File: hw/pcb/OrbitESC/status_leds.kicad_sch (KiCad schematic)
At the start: 12 parts

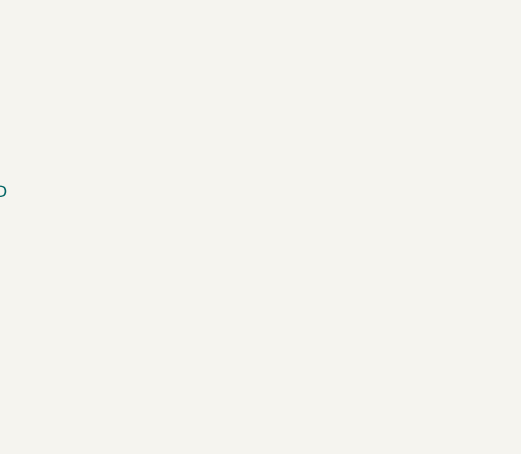
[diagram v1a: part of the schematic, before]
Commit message: Start rework of processor selection after realizing I can't afford manufacturing...
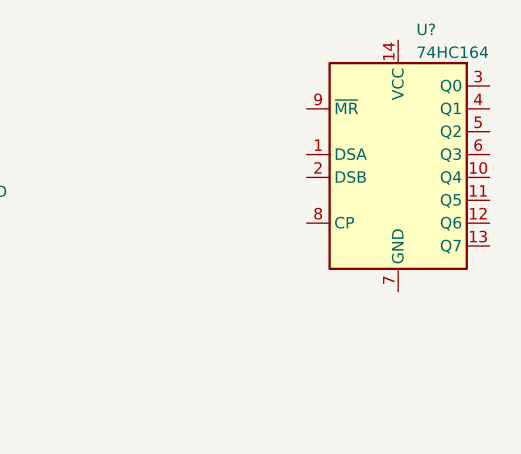
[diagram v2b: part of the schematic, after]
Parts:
- added U?: 74HC164, symbol 74xx:74HC164
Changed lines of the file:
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@@
     (pin "1")
+  )
+  (symbol (lib_id "74xx:74HC164") (at 195.58 71.12 0) (unit 1)
+    (in_bom yes) (on_board yes) (fields_autoplaced)
+    (property "Reference" "U?" (id 0) (at 197.5994 57.2602 0)
+      (effects (font (size 1.27 1.27)) (justify left))
+    )
+    (property "Value" "74HC164" (id 1) (at 197.5994 59.7971 0)
+      (effects (font (size 1.27 1.27)) (justify left))
+    )
+    (property "Footprint" "" (id 2) (at 218.44 78.74 0)
+      (effects (font (size 1.27 1.27)) hide)
+    )
+    (property "Datasheet" "https://assets.nexperia.com/documents/data-sheet/74HC_HCT164.pdf" (id 3) (at 218.44 78.74 0)
+      (effects (font (size 1.27 1.27)) hide)
+    )
+    (property "DigiKey" "MC74HC164ADR2GOSCT-ND" (id 4) (at 195.58 71.12 0)
+      (effects (font (size 1.27 1.27)) hide)
+    )
+    (pin "1")
+    (pin "10")
+    (pin "11")
+    (pin "12")
+    (pin "13")
+    (pin "14")
+    (pin "2")
+    (pin "3")
+    (pin "4")
+    (pin "5")
+    (pin "6")
+    (pin "7")
+    (pin "8")
+    (pin "9")
   )
   (symbol (lib_id "Device:LED") (at 116.84 72.39 90) (unit 1)

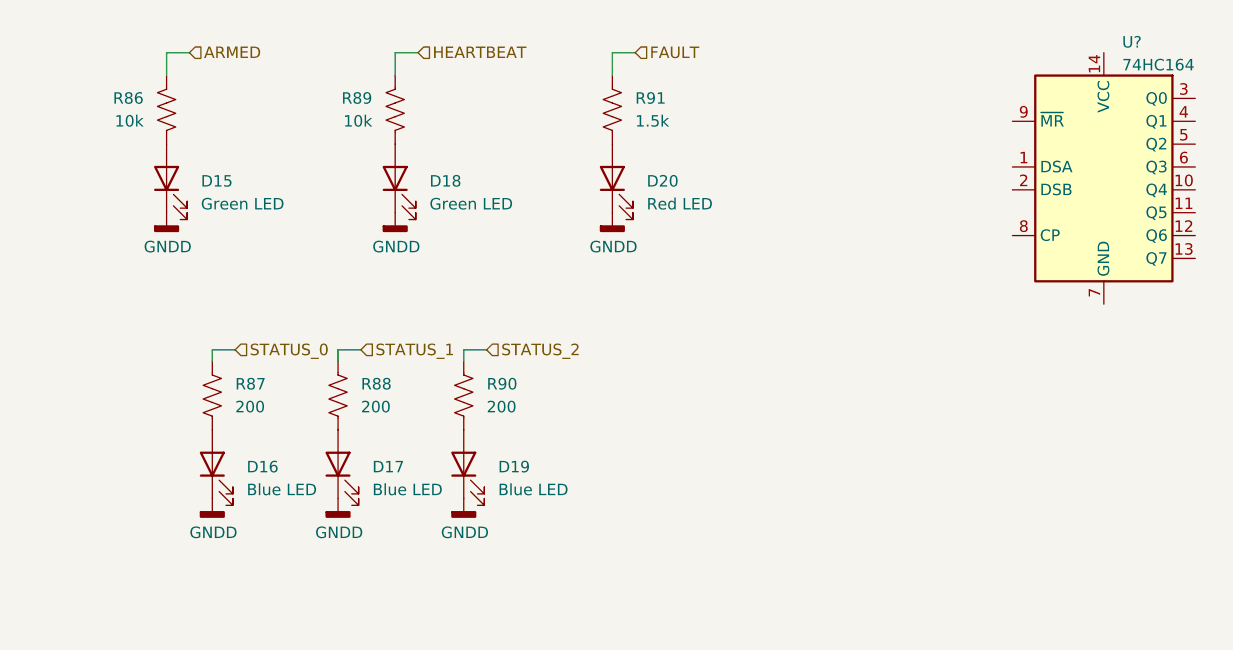
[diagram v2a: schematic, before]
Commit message: Rework new processor
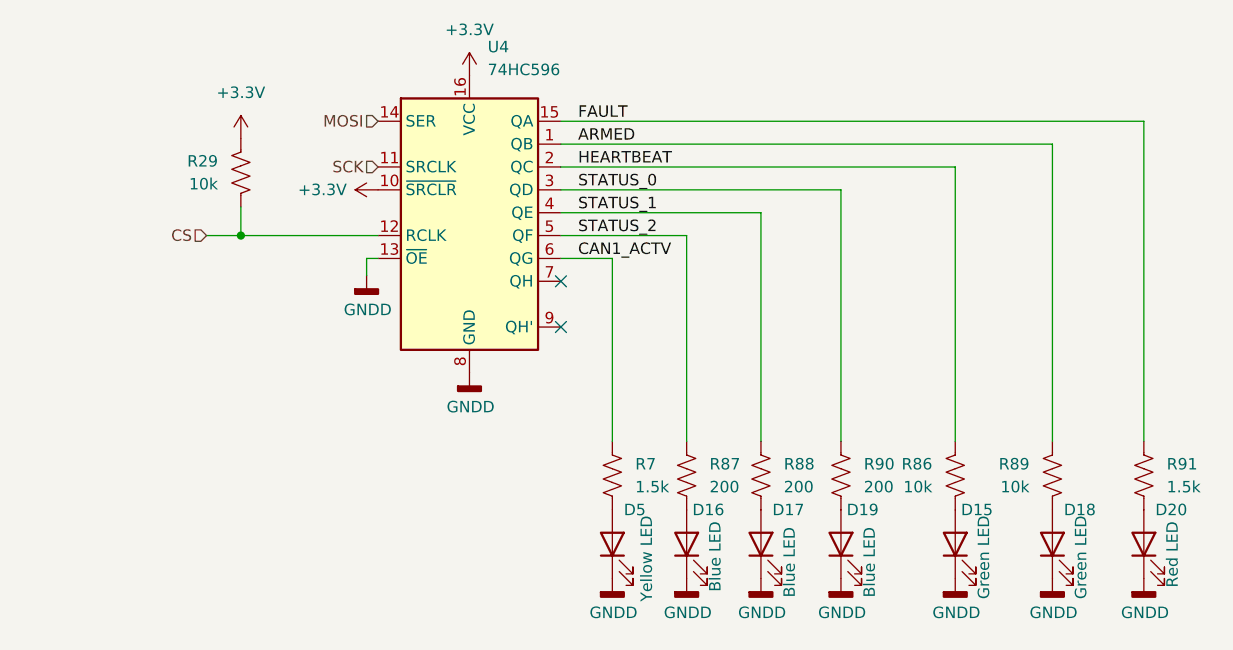
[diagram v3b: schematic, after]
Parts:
- removed U?: 74HC164, symbol 74xx:74HC164
- added D5: Yellow LED, Diode_SMD:D_0603_1608Metric, symbol Device:LED
- added R29: 10k, Resistor_SMD:R_0402_1005Metric, symbol Device:R_US
- added R7: 1.5k, Resistor_SMD:R_0402_1005Metric, symbol Device:R_US
- added U4: 74HC596, Package_SO:TSSOP-16_4.4x5mm_P0.65mm, symbol 74xx:74HC596
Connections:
- net ARMED: now also R89.2, U4.1 (QB); no longer R86.2
- net FAULT: now also U4.15 (QA)
- net GNDD: now also D5.1 (K), U4.13 (~{OE}), U4.8 (GND)
- net HEARTBEAT: now also R86.2, U4.2 (QC); no longer R89.2
- net STATUS_0: now also R90.1, U4.3 (QD); no longer R87.1
- net STATUS_1: now also U4.4 (QE)
- net STATUS_2: now also R87.1, U4.5 (QF); no longer R90.1
- new net: D5.2 (A), R7.2
- new net +3.3V: R29.2, U4.10 (~{SRCLR}), U4.16 (VCC)
- new net CAN1_ACTV: R7.1, U4.6 (QG)
- new net CS: R29.1, U4.12 (RCLK)
- new net MOSI: U4.14 (SER)
- new net SCK: U4.11 (SRCLK)
- no-connect marks 0 -> 2
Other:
- moved on the sheet: D15, D16, D17, D18, D19, D20, R86, R87, R88, R89, R90, R91

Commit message: Squash feature/sync_current_ctrl/r0
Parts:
- removed U4: 74HC596, Package_SO:TSSOP-16_4.4x5mm_P0.65mm, symbol 74xx:74HC596
- added C32: 100nF, Capacitor_SMD:C_0402_1005Metric, symbol Device:C
- added R19: 10k, Resistor_SMD:R_0402_1005Metric, symbol Device:R_US
- added U12: MC74HC595ADTR2G, Package_SO:TSSOP-16_4.4x5mm_P0.65mm, symbol 74xx:74HC595
- D15, D18: JLCPCB C72043 -> (none); LCSC (none) -> C72043
- D16, D17, D19: JLCPCB C72041 -> (none); LCSC (none) -> C72041
- D20: JLCPCB C2286 -> (none); LCSC (none) -> C2286
- D5: JLCPCB C72038 -> (none); LCSC (none) -> C72038
- R29, R86, R89: JLCPCB C25744 -> (none); LCSC (none) -> C25744
- R7: value 1.5k -> 470; JLCPCB C25867 -> (none); LCSC (none) -> C25117
- R87, R88, R90: value 200 -> 470; JLCPCB C25087 -> (none); LCSC (none) -> C25117
- R91: JLCPCB C25867 -> (none); LCSC (none) -> C25867
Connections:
- net +3.3V: now also C32.2, U12.10 (~{SRCLR}), U12.16 (VCC)
- net ARMED: now also R89.1, U12.1 (QB); no longer R89.2
- net CAN1_ACTV: now also U12.3 (QD)
- net CS: now also U12.12 (RCLK)
- net FAULT: now also U12.15 (QA)
- net GNDD: now also C32.1, R19.1, U12.8 (GND)
- net HEARTBEAT: now also R86.1, U12.2 (QC); no longer R86.2
- net MOSI: now also U12.14 (SER)
- net SCK: now also U12.11 (SRCLK)
- net STATUS_0: now also U12.4 (QE)
- net STATUS_1: now also U12.5 (QF)
- net STATUS_2: now also U12.6 (QG)
- net at D15.2 (A): now also R86.2; no longer R86.1
- net at D18.2 (A): now also R89.2; no longer R89.1
- new net OE: R19.2, U12.13 (~{OE})
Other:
- moved on the sheet: D15, D16, D17, D18, D19, D20, D5, R29, R7, R86, R87, R88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
